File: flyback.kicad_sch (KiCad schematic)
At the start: 48 parts, among them Q1 SI7898DP-T1-E3, Q2 MMBT3906, U2001 TPS23751PWP, U2002 TCMT1107, U2003 TLV431ACDBZR

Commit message: Finished routing now needs review
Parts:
- removed Q1: SI7898DP-T1-E3, footprints:MOSFET_50DP-T1-E3_VIS, symbol SI789DP-T1-E3:SI7898DP-T1-E3
- added Q2001: SI7898DP-T1-E3, footprints:MOSFET_50DP-T1-E3_VIS, symbol SI789DP-T1-E3:SI7898DP-T1-E3
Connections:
- net at R2011.1, R2013.1: now also Q2001.S
- net at D3.3 (K), Q2.2 (E), R1.1: now also Q2001.G
- net at D2.2 (A), T2001.5: now also Q2001.D
- net 5V_PRI: now reaches D1.2 (A), T2001.10, T2001.9
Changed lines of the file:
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@@
 	)
 	(junction
-		(at 212.09 88.9)
-		(diameter 0)
-		(color 0 0 0 0)
-	)
-	(junction
 		(at 121.92 135.89)
 		(diameter 0)
@@
 	)
 	(junction
-		(at 226.06 127)
+		(at 212.09 88.9)
 		(diameter 0)
 		(color 0 0 0 0)
 	)
 	(junction
-		(at 52.07 161.29)
+		(at 209.55 104.14)
 		(diameter 0)
 		(color 0 0 0 0)
 	)
 	(junction
-		(at 228.6 58.42)
+		(at 226.06 127)
 		(diameter 0)
 		(color 0 0 0 0)
 	)
 	(junction
-		(at 101.6 86.36)
+		(at 52.07 161.29)
 		(diameter 0)
 		(color 0 0 0 0)
 	)
 	(junction
-		(at 259.08 68.58)
+		(at 228.6 58.42)
 		(diameter 0)
 		(color 0 0 0 0)
 	)
 	(junction
-		(at 207.01 104.14)
+		(at 101.6 86.36)
 		(diameter 0)
 		(color 0 0 0 0)
 	)
 	(junction
-		(at 209.55 104.14)
+		(at 259.08 68.58)
 		(diameter 0)
 		(color 0 0 0 0)
@@
 	)
 	(junction
+		(at 207.01 104.14)
+		(diameter 0)
+		(color 0 0 0 0)
+	)
+	(junction
 		(at 45.72 57.15)
 		(diameter 0)
@@
 	(wire
 		(pts
+			(xy 207.01 104.14) (xy 209.55 104.14)
+		)
+		(stroke
+			(width 0)
+			(type default)
+		)
+	)
+	(wire
+		(pts
 			(xy 207.01 88.9) (xy 209.55 88.9)
 		)
@@
 	(wire
 		(pts
-			(xy 207.01 104.14) (xy 209.55 104.14)
-		)
-		(stroke
-			(width 0)
-			(type default)
-		)
-	)
-	(wire
-		(pts
 			(xy 62.23 106.68) (xy 55.88 106.68)
 		)
@@
 	(wire
 		(pts
+			(xy 209.55 88.9) (xy 212.09 88.9)
+		)
+		(stroke
+			(width 0)
+			(type default)
+		)
+	)
+	(wire
+		(pts
 			(xy 36.83 57.15) (xy 45.72 57.15)
 		)
@@
 	(wire
 		(pts
-			(xy 209.55 88.9) (xy 212.09 88.9)
-		)
-		(stroke
-			(width 0)
-			(type default)
-		)
-	)
-	(wire
-		(pts
 			(xy 196.85 83.82) (xy 196.85 88.9)
 		)
@@
 	(wire
 		(pts
-			(xy 212.09 88.9) (xy 214.63 88.9)
+			(xy 185.42 99.06) (xy 199.39 99.06)
 		)
 		(stroke
@@
 	(wire
 		(pts
-			(xy 185.42 99.06) (xy 199.39 99.06)
+			(xy 154.94 147.32) (xy 154.94 149.86)
 		)
 		(stroke
@@
 	(wire
 		(pts
-			(xy 154.94 147.32) (xy 154.94 149.86)
+			(xy 100.33 116.84) (xy 97.79 116.84)
 		)
 		(stroke
@@
 	(wire
 		(pts
-			(xy 100.33 116.84) (xy 97.79 116.84)
+			(xy 226.06 114.3) (xy 226.06 116.84)
 		)
 		(stroke
@@
 	(wire
 		(pts
-			(xy 226.06 114.3) (xy 226.06 116.84)
+			(xy 262.89 135.89) (xy 262.89 144.78)
 		)
 		(stroke
@@
 	(wire
 		(pts
-			(xy 262.89 135.89) (xy 262.89 144.78)
+			(xy 170.18 104.14) (xy 207.01 104.14)
 		)
 		(stroke
@@
 	(wire
 		(pts
-			(xy 170.18 104.14) (xy 207.01 104.14)
+			(xy 212.09 88.9) (xy 214.63 88.9)
 		)
 		(stroke
@@
 		)
 	)
+	(label "5V_PRI"
+		(at 229.87 68.58 0)
+		(fields_autoplaced yes)
+		(effects
+			(font
+				(size 1.27 1.27)
+			)
+			(justify left bottom)
+		)
+	)
 	(label "T_PRI"
 		(at 207.01 57.15 0)
@@
 	)
 	(symbol
-		(lib_id "SI789DP-T1-E3:SI7898DP-T1-E3")
-		(at 201.93 99.06 0)
-		(unit 1)
-		(exclude_from_sim no)
-		(in_bom yes)
-		(on_board yes)
-		(dnp no)
-		(fields_autoplaced yes)
-		(property "Reference" "Q1"
-			(at 215.9 95.2499 0)
-			(effects
-				(font
-					(size 1.524 1.524)
-				)
-				(justify left)
-			)
-		)
-		(property "Value" "SI7898DP-T1-E3"
-			(at 215.9 97.7899 0)
-			(effects
-				(font
-					(size 1.524 1.524)
-				)
-				(justify left)
-			)
-		)
-		(property "Footprint" "footprints:MOSFET_50DP-T1-E3_VIS"
-			(at 201.93 99.06 0)
-			(effects
-				(font
-					(size 1.27 1.27)
-					(italic yes)
-				)
-				(hide yes)
-			)
-		)
-		(property "Datasheet" "SI7898DP-T1-E3"
-			(at 201.93 99.06 0)
-			(effects
-				(font
-					(size 1.27 1.27)
-					(italic yes)
-				)
-				(hide yes)
-			)
-		)
-		(property "Description" ""
-			(at 201.93 99.06 0)
-			(effects
-				(font
-					(size 1.27 1.27)
-				)
-				(hide yes)
-			)
-		)
-		(pin "8"
-		)
-		(pin "6"
-		)
-		(pin "7"
-		)
-		(pin "2"
-		)
-		(pin "1"
-		)
-		(pin "3"
-		)
-		(pin "5"
-		)
-		(pin "4"
-		)
-		(instances
-			(project ""
-				(path "/e8d70991-5081-4afb-b8c3-5ce9f62355e0/1fdbb5e2-ecd4-47ea-a63c-f2f18c06d291"
-					(reference "Q1")
-					(unit 1)
-				)
-			)
-		)
-	)
-	(symbol
 		(lib_id "power:GND")
 		(at 50.8 124.46 0)
@@
 					(unit 1)
 				)
+			)
+		)
+	)
+	(symbol
+		(lib_id "SI789DP-T1-E3:SI7898DP-T1-E3")
+		(at 201.93 99.06 0)
+		(unit 1)
+		(exclude_from_sim no)
+		(in_bom yes)
+		(on_board yes)
+		(dnp no)
+		(fields_autoplaced yes)
+		(property "Reference" "Q2001"
+			(at 215.9 95.2499 0)
+			(effects
+				(font
+					(size 1.524 1.524)
+				)
+				(justify left)
+			)
+		)
+		(property "Value" "SI7898DP-T1-E3"
+			(at 215.9 97.7899 0)
+			(effects
+				(font
+					(size 1.524 1.524)
+				)
+				(justify left)
+			)
+		)
+		(property "Footprint" "footprints:MOSFET_50DP-T1-E3_VIS"
+			(at 201.93 99.06 0)
+			(effects
+				(font
+					(size 1.27 1.27)
+					(italic yes)
+				)
+				(hide yes)
+			)
+		)
+		(property "Datasheet" "SI7898DP-T1-E3"
+			(at 201.93 99.06 0)
+			(effects
+				(font
+					(size 1.27 1.27)
+					(italic yes)
+				)
+				(hide yes)
+			)
+		)
+		(property "Description" ""
+			(at 201.93 99.06 0)
+			(effects
+				(font
+					(size 1.27 1.27)
+				)
+				(hide yes)
+			)
+		)
+		(pin "D"
+		)
+		(pin "D"
+		)
+		(pin "G"
+		)
+		(pin "S"
+		)
+		(pin "D"
+		)
+		(pin "S"
+		)
+		(pin "D"
+		)
+		(pin "S"
+		)
+		(instances
+			(project ""
+				(path "/e8d70991-5081-4afb-b8c3-5ce9f62355e0/1fdbb5e2-ecd4-47ea-a63c-f2f18c06d291"
+					(reference "Q2001")
+					(unit 1)
+				)

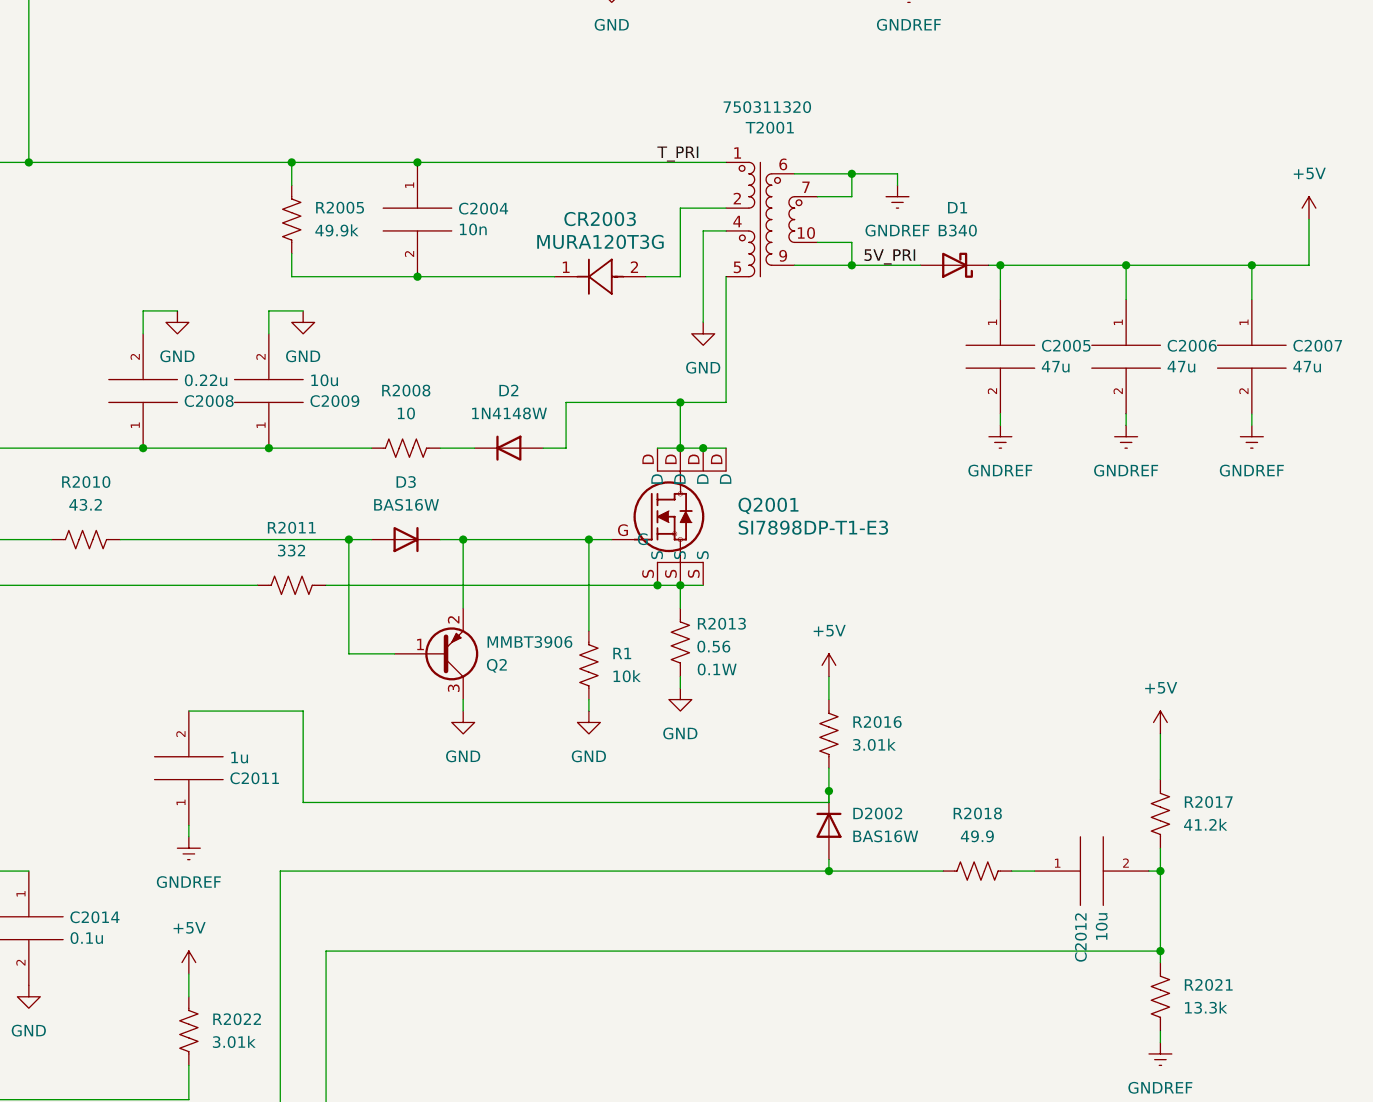
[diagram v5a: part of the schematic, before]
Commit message: Added buck
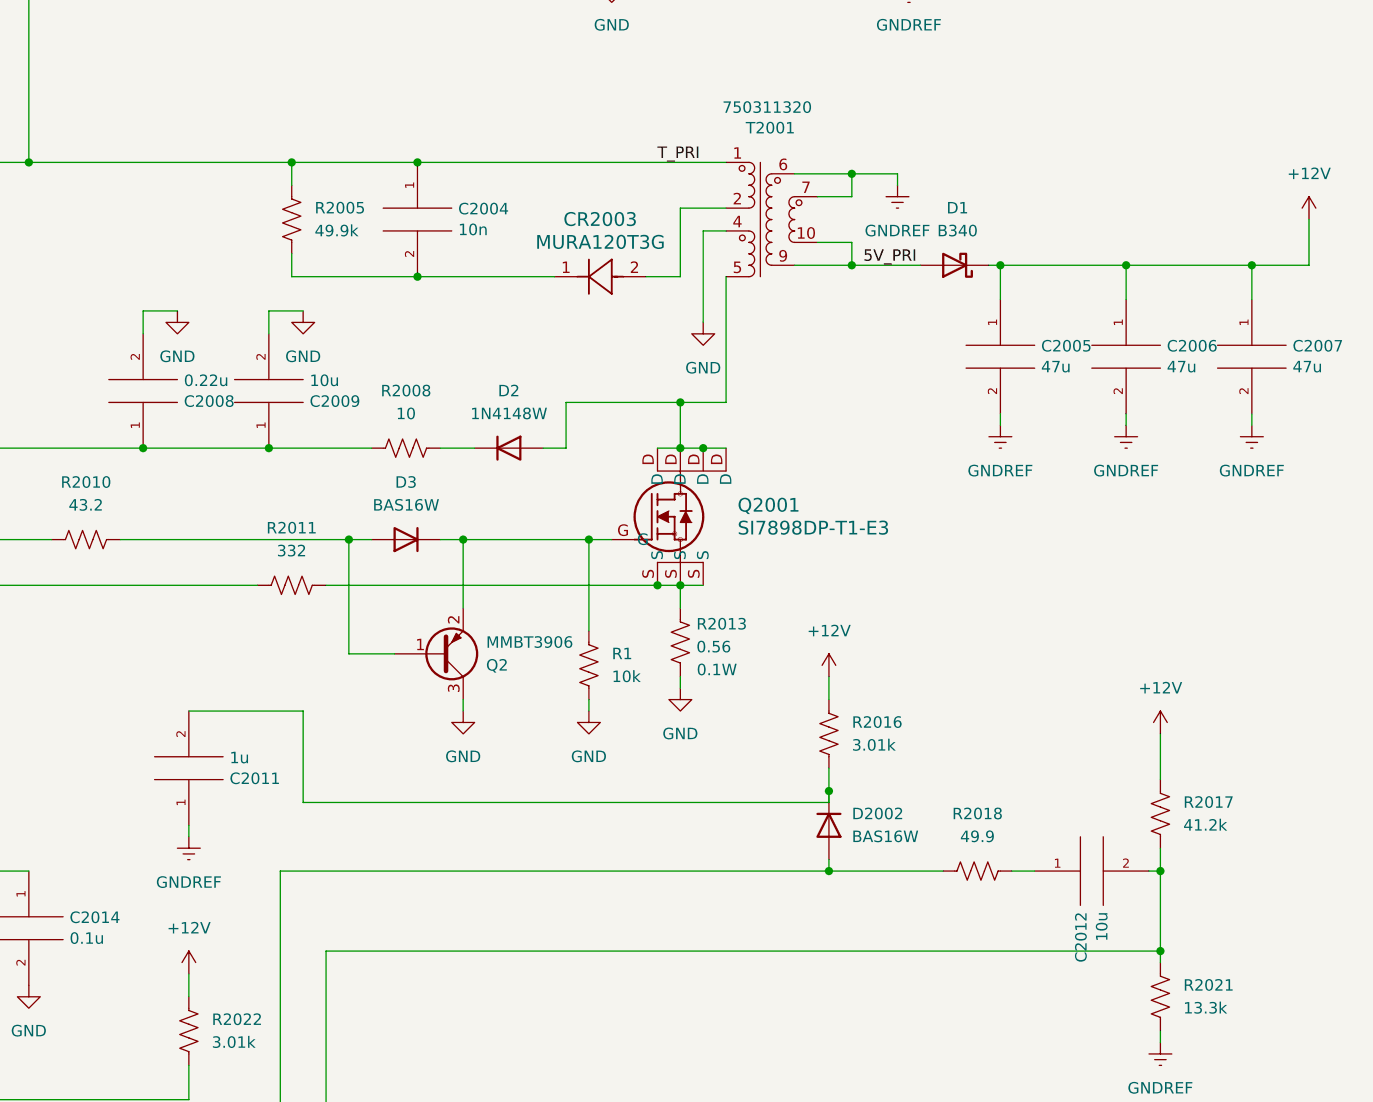
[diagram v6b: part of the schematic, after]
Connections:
- net +5V renamed +12V
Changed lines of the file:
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@@
+	)
+	(symbol
+		(lib_id "power:+12V")
+		(at 262.89 120.65 0)
+		(unit 1)
+		(exclude_from_sim no)
+		(in_bom yes)
+		(on_board yes)
+		(dnp no)
+		(fields_autoplaced yes)
+		(property "Reference" "#PWR05"
+			(at 262.89 124.46 0)
+			(effects
+				(font
+					(size 1.27 1.27)
+				)
+				(hide yes)
+			)
+		)
+		(property "Value" "+12V"
+			(at 262.89 115.57 0)
+			(effects
+				(font
+					(size 1.27 1.27)
+				)
+			)
+		)
+		(property "Footprint" ""
+			(at 262.89 120.65 0)
+			(effects
+				(font
+					(size 1.27 1.27)
+				)
+				(hide yes)
+			)
+		)
+		(property "Datasheet" ""
+			(at 262.89 120.65 0)
+			(effects
+				(font
+					(size 1.27 1.27)
+				)
+				(hide yes)
+			)
+		)
+		(property "Description" "Power symbol creates a global label with name \"+12V\""
+			(at 262.89 120.65 0)
+			(effects
+				(font
+					(size 1.27 1.27)
+				)
+				(hide yes)
+			)
+		)
+		(pin "1"
+		)
+		(instances
+			(project "PoE"
+				(path "/e8d70991-5081-4afb-b8c3-5ce9f62355e0/1fdbb5e2-ecd4-47ea-a63c-f2f18c06d291"
+					(reference "#PWR05")
+					(unit 1)
+				)
+			)
+		)
 	)
 	(symbol
@@
 	)
 	(symbol
+		(lib_id "power:+12V")
+		(at 279.4 63.5 0)
+		(unit 1)
+		(exclude_from_sim no)
+		(in_bom yes)
+		(on_board yes)
+		(dnp no)
+		(fields_autoplaced yes)
+		(property "Reference" "#PWR06"
+			(at 279.4 67.31 0)
+			(effects
+				(font
+					(size 1.27 1.27)
+				)
+				(hide yes)
+			)
+		)
+		(property "Value" "+12V"
+			(at 279.4 58.42 0)
+			(effects
+				(font
+					(size 1.27 1.27)
+				)
+			)
+		)
+		(property "Footprint" ""
+			(at 279.4 63.5 0)
+			(effects
+				(font
+					(size 1.27 1.27)
+				)
+				(hide yes)
+			)
+		)
+		(property "Datasheet" ""
+			(at 279.4 63.5 0)
+			(effects
+				(font
+					(size 1.27 1.27)
+				)
+				(hide yes)
+			)
+		)
+		(property "Description" "Power symbol creates a global label with name \"+12V\""
+			(at 279.4 63.5 0)
+			(effects
+				(font
+					(size 1.27 1.27)
+				)
+				(hide yes)
+			)
+		)
+		(pin "1"
+		)
+		(instances
+			(project "PoE"
+				(path "/e8d70991-5081-4afb-b8c3-5ce9f62355e0/1fdbb5e2-ecd4-47ea-a63c-f2f18c06d291"
+					(reference "#PWR06")
+					(unit 1)
+				)
+			)
+		)
+	)
+	(symbol
 		(lib_id "Device:R_US")
 		(at 143.51 99.06 270)
@@
 	)
 	(symbol
-		(lib_id "power:+5V")
-		(at 279.4 63.5 0)
+		(lib_id "power:+12V")
+		(at 154.94 147.32 0)
 		(unit 1)
 		(exclude_from_sim no)
@@
 		(dnp no)
 		(fields_autoplaced yes)
-		(property "Reference" "#PWR02007"
-			(at 279.4 67.31 0)
-			(effects
-				(font
-					(size 1.27 1.27)
-				)
-				(hide yes)
-			)
-		)
-		(property "Value" "+5V"
-			(at 279.4 58.42 0)
+		(property "Reference" "#PWR03"
+			(at 154.94 151.13 0)
+			(effects
+				(font
+					(size 1.27 1.27)
+				)
+				(hide yes)
+			)
+		)
+		(property "Value" "+12V"
+			(at 154.94 142.24 0)
 			(effects
 				(font
@@
 		)
 		(property "Footprint" ""
-			(at 279.4 63.5 0)
+			(at 154.94 147.32 0)
 			(effects
 				(font
@@
 		)
 		(property "Datasheet" ""
-			(at 279.4 63.5 0)
-			(effects
-				(font
-					(size 1.27 1.27)
-				)
-				(hide yes)
-			)
-		)
-		(property "Description" "Power symbol creates a global label with name \"+5V\""
-			(at 279.4 63.5 0)
+			(at 154.94 147.32 0)
+			(effects
+				(font
+					(size 1.27 1.27)
+				)
+				(hide yes)
+			)
+		)
+		(property "Description" "Power symbol creates a global label with name \"+12V\""
+			(at 154.94 147.32 0)
 			(effects
 				(font
@@
 			(project ""
 				(path "/e8d70991-5081-4afb-b8c3-5ce9f62355e0/1fdbb5e2-ecd4-47ea-a63c-f2f18c06d291"
-					(reference "#PWR02007")
+					(reference "#PWR03")
 					(unit 1)
 				)
@@
 	)
 	(symbol
-		(lib_id "power:+5V")
-		(at 262.89 120.65 0)
+		(lib_id "power:+12V")
+		(at 226.06 114.3 0)
 		(unit 1)
 		(exclude_from_sim no)
@@
 		(dnp no)
 		(fields_autoplaced yes)
-		(property "Reference" "#PWR02018"
-			(at 262.89 124.46 0)
-			(effects
-				(font
-					(size 1.27 1.27)
-				)
-				(hide yes)
-			)
-		)
-		(property "Value" "+5V"
-			(at 262.89 115.57 0)
+		(property "Reference" "#PWR04"
+			(at 226.06 118.11 0)
+			(effects
+				(font
+					(size 1.27 1.27)
+				)
+				(hide yes)
+			)
+		)
+		(property "Value" "+12V"
+			(at 226.06 109.22 0)
 			(effects
 				(font
@@
 		)
 		(property "Footprint" ""
-			(at 262.89 120.65 0)
+			(at 226.06 114.3 0)
 			(effects
 				(font
@@
 		)
 		(property "Datasheet" ""
-			(at 262.89 120.65 0)
-			(effects
-				(font
-					(size 1.27 1.27)
-				)
-				(hide yes)
-			)
-		)
-		(property "Description" "Power symbol creates a global label with name \"+5V\""
-			(at 262.89 120.65 0)
-			(effects
-				(font
-					(size 1.27 1.27)
-				)
-				(hide yes)
-			)
-		)
-		(pin "1"
-		)
-		(instances
-			(project "PoE"
-				(path "/e8d70991-5081-4afb-b8c3-5ce9f62355e0/1fdbb5e2-ecd4-47ea-a63c-f2f18c06d291"
-					(reference "#PWR02018")
+			(at 226.06 114.3 0)
+			(effects
+				(font
+					(size 1.27 1.27)
+				)
+				(hide yes)
+			)
+		)
+		(property "Description" "Power symbol creates a global label with name \"+12V\""
+			(at 226.06 114.3 0)
+			(effects
+				(font
+					(size 1.27 1.27)
+				)
+				(hide yes)
+			)
+		)
+		(pin "1"
+		)
+		(instances
+			(project "PoE"
+				(path "/e8d70991-5081-4afb-b8c3-5ce9f62355e0/1fdbb5e2-ecd4-47ea-a63c-f2f18c06d291"
+					(reference "#PWR04")
 					(unit 1)
 				)
@@
 	)
 	(symbol
-		(lib_id "power:+5V")
-		(at 226.06 114.3 0)
-		(unit 1)
-		(exclude_from_sim no)
-		(in_bom yes)
-		(on_board yes)
-		(dnp no)
-		(fields_autoplaced yes)
-		(property "Reference" "#PWR02016"
-			(at 226.06 118.11 0)
-			(effects
-				(font
-					(size 1.27 1.27)
-				)
-				(hide yes)
-			)
-		)
-		(property "Value" "+5V"
-			(at 226.06 109.22 0)
-			(effects
-				(font
-					(size 1.27 1.27)
-				)
-			)
-		)
-		(property "Footprint" ""
-			(at 226.06 114.3 0)
-			(effects
-				(font
-					(size 1.27 1.27)
-				)
-				(hide yes)
-			)
-		)
-		(property "Datasheet" ""
-			(at 226.06 114.3 0)
-			(effects
-				(font
-					(size 1.27 1.27)
-				)
-				(hide yes)
-			)
-		)
-		(property "Description" "Power symbol creates a global label with name \"+5V\""
-			(at 226.06 114.3 0)
-			(effects
-				(font
-					(size 1.27 1.27)
-				)
-				(hide yes)
-			)
-		)
-		(pin "1"
-		)
-		(instances
-			(project ""
-				(path "/e8d70991-5081-4afb-b8c3-5ce9f62355e0/1fdbb5e2-ecd4-47ea-a63c-f2f18c06d291"
-					(reference "#PWR02016")
-					(unit 1)
-				)
-			)
-		)
-	)
-	(symbol
 		(lib_id "Device:R_US")
 		(at 111.76 139.7 270)
@@
 					(unit 1)
 				)
-			)
-		)
-	)
-	(symbol
-		(lib_id "power:+5V")
-		(at 154.94 147.32 0)
-		(unit 1)
-		(exclude_from_sim no)
-		(in_bom yes)
-		(on_board yes)
-		(dnp no)
-		(fields_autoplaced yes)
-		(property "Reference" "#PWR02024"
-			(at 154.94 151.13 0)
-			(effects
-				(font
-					(size 1.27 1.27)
-				)
-				(hide yes)
-			)
-		)
-		(property "Value" "+5V"
-			(at 154.94 142.24 0)
-			(effects
-				(font
-					(size 1.27 1.27)
-				)
-			)
-		)
-		(property "Footprint" ""
-			(at 154.94 147.32 0)
-			(effects
-				(font
-					(size 1.27 1.27)
-				)
-				(hide yes)
-			)
-		)
-		(property "Datasheet" ""
-			(at 154.94 147.32 0)
-			(effects
-				(font
-					(size 1.27 1.27)
-				)
-				(hide yes)
-			)
-		)
-		(property "Description" "Power symbol creates a global label with name \"+5V\""
-			(at 154.94 147.32 0)
-			(effects
-				(font
-					(size 1.27 1.27)
-				)
-				(hide yes)
-			)
-		)
-		(pin "1"
-		)
-		(instances
-			(project "PoE"
-				(path "/e8d70991-5081-4afb-b8c3-5ce9f62355e0/1fdbb5e2-ecd4-47ea-a63c-f2f18c06d291"
-					(reference "#PWR02024")
-					(unit 1)
-				)

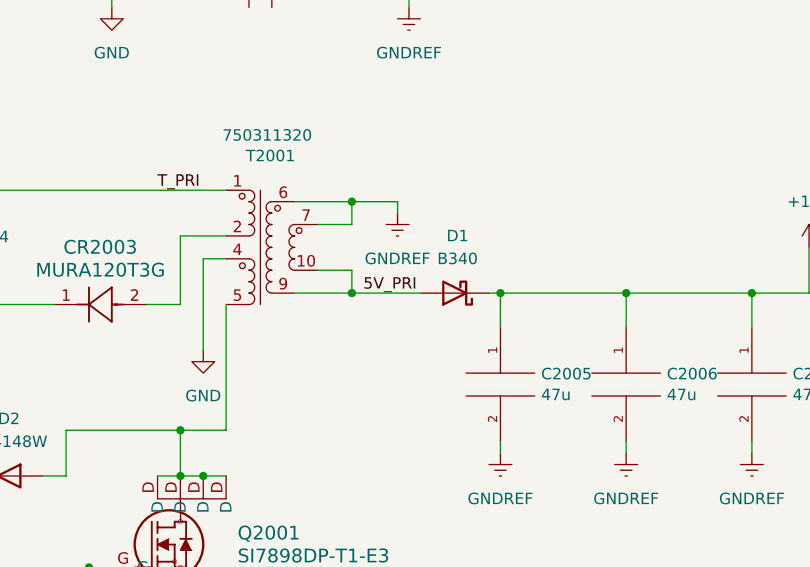
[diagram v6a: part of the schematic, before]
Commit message: Updated layout and constraints
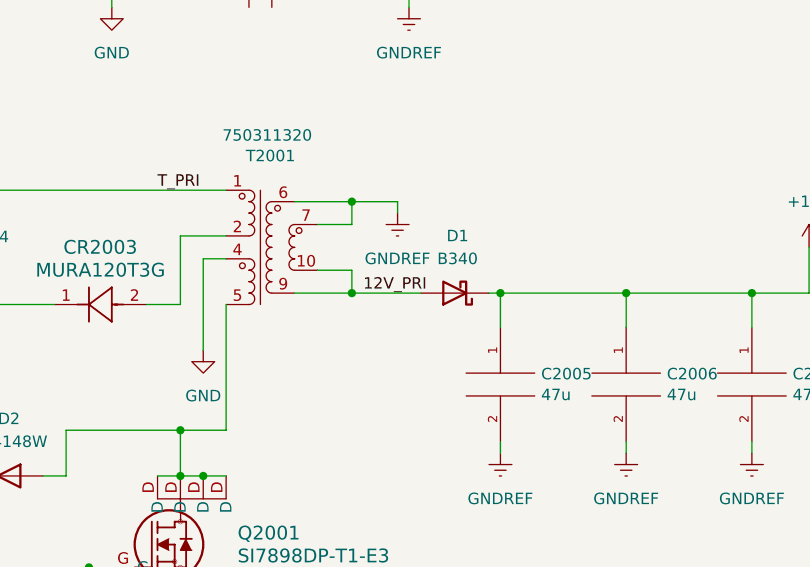
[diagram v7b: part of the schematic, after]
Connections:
- net 5V_PRI renamed 12V_PRI
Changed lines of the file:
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@@
 		)
 	)
-	(label "5V_PRI"
+	(label "12V_PRI"
 		(at 229.87 68.58 0)
 		(fields_autoplaced yes)

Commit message: Minor changes
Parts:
- R2009: value 63..4k -> 63.4k
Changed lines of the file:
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@@
 			)
 		)
-		(property "Value" "63..4k"
+		(property "Value" "63.4k"
 			(at 29.21 99.0599 0)
 			(effects
